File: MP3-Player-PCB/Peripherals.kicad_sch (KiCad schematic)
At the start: 27 parts, among them J301 Micro_SD_Card_Det1, Q301 AO3401A, Q302 2N7002H, SW301 1-1825910-4, SW302 1-1825910-4, SW303 1-1825910-4, SW304 1-1825910-4, U301 TPD4E1U06

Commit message: Assigned all footprints
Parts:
- J301: footprint (none) -> MP3-Player_Footprint_Libraries:TF-015
- R301, R302, R303, R304, R308, R309, R310, R311, R312: footprint (none) -> Resistor_SMD:R_0402_1005Metric
- R305, R306, R307: footprint (none) -> Resistor_SMD:R_0603_1608Metric
- SW301, SW302, SW303, SW304: footprint (none) -> MP3-Player_Footprint_Libraries:1-1825910-4
- U301: footprint (none) -> Package_TO_SOT_SMD:SOT-23-5
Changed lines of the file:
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@@
 			)
 		)
-		(property "Footprint" ""
+		(property "Footprint" "Resistor_SMD:R_0402_1005Metric"
 			(at 60.452 113.03 90)
 			(effects
@@
 			)
 		)
-		(property "Footprint" ""
+		(property "Footprint" "MP3-Player_Footprint_Libraries:TF-015"
 			(at 193.04 33.02 0)
 			(effects
@@
 			)
 		)
-		(property "Footprint" ""
+		(property "Footprint" "MP3-Player_Footprint_Libraries:1-1825910-4"
 			(at 270.51 36.83 0)
 			(effects
@@
 			)
 		)
-		(property "Footprint" ""
+		(property "Footprint" "MP3-Player_Footprint_Libraries:1-1825910-4"
 			(at 220.98 55.88 0)
 			(effects
@@
 			)
 		)
-		(property "Footprint" ""
+		(property "Footprint" "MP3-Player_Footprint_Libraries:1-1825910-4"
 			(at 270.51 55.88 0)
 			(effects
@@
 			)
 		)
-		(property "Footprint" ""
+		(property "Footprint" "Package_TO_SOT_SMD:SOT-23-5"
 			(at 128.27 81.28 0)
 			(effects
@@
 			)
 		)
-		(property "Footprint" ""
+		(property "Footprint" "Resistor_SMD:R_0402_1005Metric"
 			(at 201.422 55.88 90)
 			(effects
@@
 			)
 		)
-		(property "Footprint" ""
+		(property "Footprint" "Resistor_SMD:R_0402_1005Metric"
 			(at 201.422 36.83 90)
 			(effects
@@
 			)
 		)
-		(property "Footprint" ""
+		(property "Footprint" "Resistor_SMD:R_0402_1005Metric"
 			(at 73.152 36.83 90)
 			(effects
@@
 			)
 		)
-		(property "Footprint" ""
+		(property "Footprint" "Resistor_SMD:R_0402_1005Metric"
 			(at 250.952 36.83 90)
 			(effects
@@
 			)
 		)
-		(property "Footprint" ""
+		(property "Footprint" "Resistor_SMD:R_0402_1005Metric"
 			(at 250.952 55.88 90)
 			(effects
@@
 			)
 		)
-		(property "Footprint" ""
+		(property "Footprint" "Resistor_SMD:R_0603_1608Metric"
 			(at 91.44 47.498 90)
 			(effects
@@
 			)
 		)
-		(property "Footprint" ""
+		(property "Footprint" "Resistor_SMD:R_0603_1608Metric"
 			(at 91.44 57.658 90)
 			(effects
@@
 			)
 		)
-		(property "Footprint" ""
+		(property "Footprint" "Resistor_SMD:R_0402_1005Metric"
 			(at 82.042 36.83 90)
 			(effects
@@
 			)
 		)
-		(property "Footprint" ""
+		(property "Footprint" "Resistor_SMD:R_0402_1005Metric"
 			(at 60.452 67.31 90)
 			(effects
@@
 			)
 		)
-		(property "Footprint" ""
+		(property "Footprint" "MP3-Player_Footprint_Libraries:1-1825910-4"
 			(at 220.98 36.83 0)
 			(effects
@@
 			)
 		)
-		(property "Footprint" ""
+		(property "Footprint" "Resistor_SMD:R_0402_1005Metric"
 			(at 47.752 132.08 90)
 			(effects
@@
 			)
 		)
-		(property "Footprint" ""
+		(property "Footprint" "Resistor_SMD:R_0603_1608Metric"
 			(at 91.44 52.578 90)
 			(effects

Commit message: Fixed all ERC errors
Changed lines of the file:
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@@
 	)
 	(junction
+		(at 63.5 107.95)
+		(diameter 0)
+		(color 0 0 0 0)
+	)
+	(junction
 		(at 121.92 128.27)
 		(diameter 0)
@@
 	(wire
 		(pts
+			(xy 63.5 107.95) (xy 72.39 107.95)
+		)
+		(stroke
+			(width 0)
+			(type default)
+		)
+	)
+	(wire
+		(pts
 			(xy 83.82 40.64) (xy 83.82 45.72)
 		)
@@
 	(wire
 		(pts
-			(xy 62.23 107.95) (xy 72.39 107.95)
+			(xy 62.23 107.95) (xy 63.5 107.95)
 		)
 		(stroke
@@
 	)
 	(symbol
+		(lib_id "power:PWR_FLAG")
+		(at 63.5 107.95 0)
+		(unit 1)
+		(exclude_from_sim no)
+		(in_bom yes)
+		(on_board yes)
+		(dnp no)
+		(fields_autoplaced yes)
+		(property "Reference" "#FLG0301"
+			(at 63.5 106.045 0)
+			(effects
+				(font
+					(size 1.27 1.27)
+				)
+				(hide yes)
+			)
+		)
+		(property "Value" "PWR_FLAG"
+			(at 63.5 102.87 0)
+			(effects
+				(font
+					(size 1.27 1.27)
+				)
+			)
+		)
+		(property "Footprint" ""
+			(at 63.5 107.95 0)
+			(effects
+				(font
+					(size 1.27 1.27)
+				)
+				(hide yes)
+			)
+		)
+		(property "Datasheet" "~"
+			(at 63.5 107.95 0)
+			(effects
+				(font
+					(size 1.27 1.27)
+				)
+				(hide yes)
+			)
+		)
+		(property "Description" "Special symbol for telling ERC where power comes from"
+			(at 63.5 107.95 0)
+			(effects
+				(font
+					(size 1.27 1.27)
+				)
+				(hide yes)
+			)
+		)
+		(pin "1"
+		)
+		(instances
+			(project "MP3-Player"
+				(path "/3f51ea9b-d2e1-4711-a47c-269e1b97e0f4/425fb02a-335c-42f3-aa7e-942bbee7b5dd"
+					(reference "#FLG0301")
+					(unit 1)
+				)
+			)
+		)
+	)
+	(symbol
 		(lib_id "power:GND")
 		(at 62.23 134.62 0)
@@
 					(unit 1)
 				)
+			)
+		)
+	)
+	(symbol
+		(lib_id "power:PWR_FLAG")
+		(at 121.92 128.27 0)
+		(unit 1)
+		(exclude_from_sim no)
+		(in_bom yes)
+		(on_board yes)
+		(dnp no)
+		(fields_autoplaced yes)
+		(property "Reference" "#FLG0302"
+			(at 121.92 126.365 0)
+			(effects
+				(font
+					(size 1.27 1.27)
+				)
+				(hide yes)
+			)
+		)
+		(property "Value" "PWR_FLAG"
+			(at 121.92 123.19 0)
+			(effects
+				(font
+					(size 1.27 1.27)
+				)
+			)
+		)
+		(property "Footprint" ""
+			(at 121.92 128.27 0)
+			(effects
+				(font
+					(size 1.27 1.27)
+				)
+				(hide yes)
+			)
+		)
+		(property "Datasheet" "~"
+			(at 121.92 128.27 0)
+			(effects
+				(font
+					(size 1.27 1.27)
+				)
+				(hide yes)
+			)
+		)
+		(property "Description" "Special symbol for telling ERC where power comes from"
+			(at 121.92 128.27 0)
+			(effects
+				(font
+					(size 1.27 1.27)
+				)
+				(hide yes)
+			)
+		)
+		(pin "1"
+		)
+		(instances
+			(project "MP3-Player"
+				(path "/3f51ea9b-d2e1-4711-a47c-269e1b97e0f4/425fb02a-335c-42f3-aa7e-942bbee7b5dd"
+					(reference "#FLG0302")
+					(unit 1)
+				)

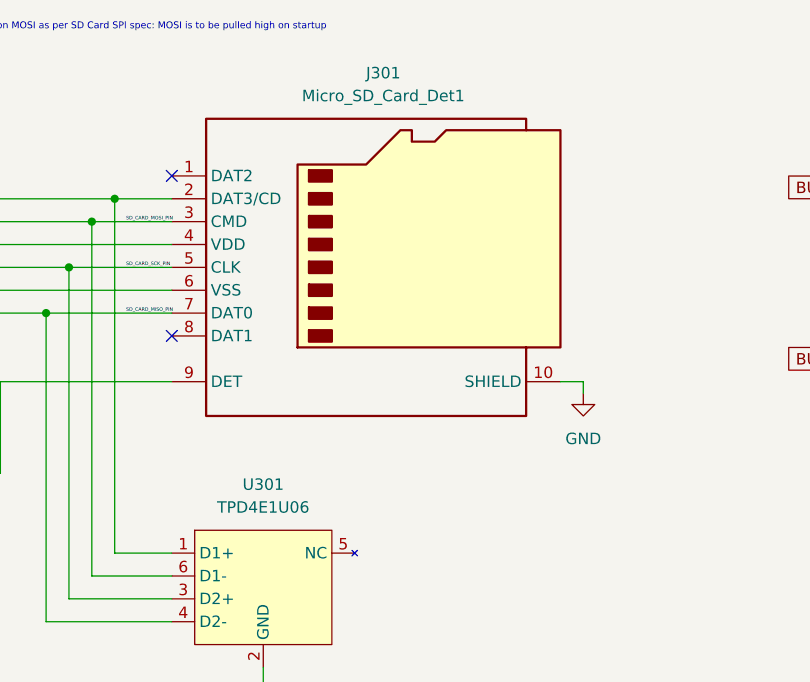
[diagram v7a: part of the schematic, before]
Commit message: Fixed all import change from schematic errors and warnings
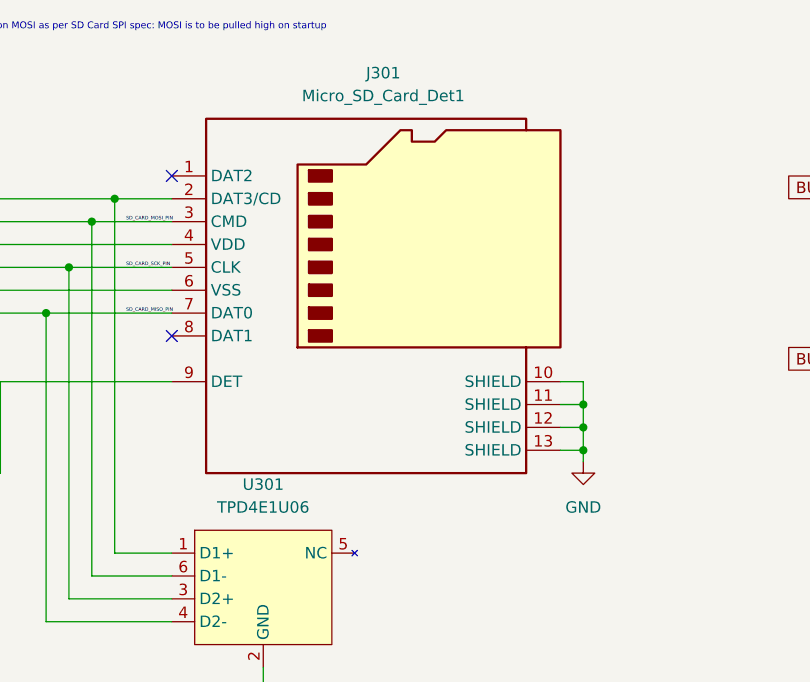
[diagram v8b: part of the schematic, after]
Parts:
- U301: footprint Package_TO_SOT_SMD:SOT-23-5 -> Package_TO_SOT_SMD:SOT-23-6
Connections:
- net GND: now also J301.11 (SHIELD), J301.12 (SHIELD), J301.13 (SHIELD)
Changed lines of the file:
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@@
+	)
+	(junction
+		(at 163.83 66.04)
+		(diameter 0)
+		(color 0 0 0 0)
 	)
 	(junction
@@
 	)
 	(junction
+		(at 163.83 68.58)
+		(diameter 0)
+		(color 0 0 0 0)
+	)
+	(junction
 		(at 111.76 43.18)
 		(diameter 0)
@@
 	(junction
 		(at 43.18 48.26)
+		(diameter 0)
+		(color 0 0 0 0)
+	)
+	(junction
+		(at 163.83 71.12)
 		(diameter 0)
 		(color 0 0 0 0)
@@
 	(wire
 		(pts
+			(xy 163.83 63.5) (xy 163.83 66.04)
+		)
+		(stroke
+			(width 0)
+			(type default)
+		)
+	)
+	(wire
+		(pts
 			(xy 228.6 60.96) (xy 228.6 63.5)
 		)
@@
 	(wire
 		(pts
+			(xy 161.29 68.58) (xy 163.83 68.58)
+		)
+		(stroke
+			(width 0)
+			(type default)
+		)
+	)
+	(wire
+		(pts
 			(xy 106.68 87.63) (xy 106.68 50.8)
 		)
@@
 	(wire
 		(pts
+			(xy 161.29 66.04) (xy 163.83 66.04)
+		)
+		(stroke
+			(width 0)
+			(type default)
+		)
+	)
+	(wire
+		(pts
 			(xy 62.23 71.12) (xy 62.23 73.66)
 		)
@@
 	(wire
 		(pts
+			(xy 161.29 71.12) (xy 163.83 71.12)
+		)
+		(stroke
+			(width 0)
+			(type default)
+		)
+	)
+	(wire
+		(pts
 			(xy 72.39 142.24) (xy 81.28 142.24)
 		)
@@
 	(wire
 		(pts
+			(xy 163.83 66.04) (xy 163.83 68.58)
+		)
+		(stroke
+			(width 0)
+			(type default)
+		)
+	)
+	(wire
+		(pts
 			(xy 95.25 55.88) (xy 104.14 55.88)
 		)
@@
 	(wire
 		(pts
+			(xy 163.83 71.12) (xy 163.83 68.58)
+		)
+		(stroke
+			(width 0)
+			(type default)
+		)
+	)
+	(wire
+		(pts
 			(xy 30.48 58.42) (xy 30.48 62.23)
 		)
@@
 	(wire
 		(pts
-			(xy 163.83 64.77) (xy 163.83 63.5)
+			(xy 163.83 72.39) (xy 163.83 71.12)
 		)
 		(stroke
@@
 	(symbol
 		(lib_id "power:GND")
-		(at 163.83 64.77 0)
+		(at 163.83 72.39 0)
 		(unit 1)
 		(exclude_from_sim no)
@@
 		(fields_autoplaced yes)
 		(property "Reference" "#PWR0316"
-			(at 163.83 71.12 0)
+			(at 163.83 78.74 0)
 			(effects
 				(font
@@
 		)
 		(property "Value" "GND"
-			(at 163.83 69.85 0)
+			(at 163.83 77.47 0)
 			(effects
 				(font
@@
 		)
 		(property "Footprint" ""
-			(at 163.83 64.77 0)
+			(at 163.83 72.39 0)
 			(effects
 				(font
@@
 		)
 		(property "Datasheet" ""
-			(at 163.83 64.77 0)
+			(at 163.83 72.39 0)
 			(effects
 				(font
@@
 		)
 		(property "Description" "Power symbol creates a global label with name \"GND\" , ground"
-			(at 163.83 64.77 0)
+			(at 163.83 72.39 0)
 			(effects
 				(font
@@
 			)
 		)
+		(pin "12"
+		)
+		(pin "4"
+		)
+		(pin "8"
+		)
+		(pin "5"
+		)
+		(pin "6"
+		)
+		(pin "1"
+		)
+		(pin "7"
+		)
+		(pin "3"
+		)
+		(pin "9"
+		)
+		(pin "2"
+		)
+		(pin "13"
+		)
 		(pin "10"
 		)
-		(pin "4"
-		)
-		(pin "8"
-		)
-		(pin "5"
-		)
-		(pin "6"
-		)
-		(pin "1"
-		)
-		(pin "7"
-		)
-		(pin "3"
-		)
-		(pin "9"
-		)
-		(pin "2"
+		(pin "11"
 		)
 		(instances
@@
 			)
 		)
-		(property "Footprint" "Package_TO_SOT_SMD:SOT-23-5"
+		(property "Footprint" "Package_TO_SOT_SMD:SOT-23-6"
 			(at 128.27 81.28 0)
 			(effects
